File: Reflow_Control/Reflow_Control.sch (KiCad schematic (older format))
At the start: 35 parts

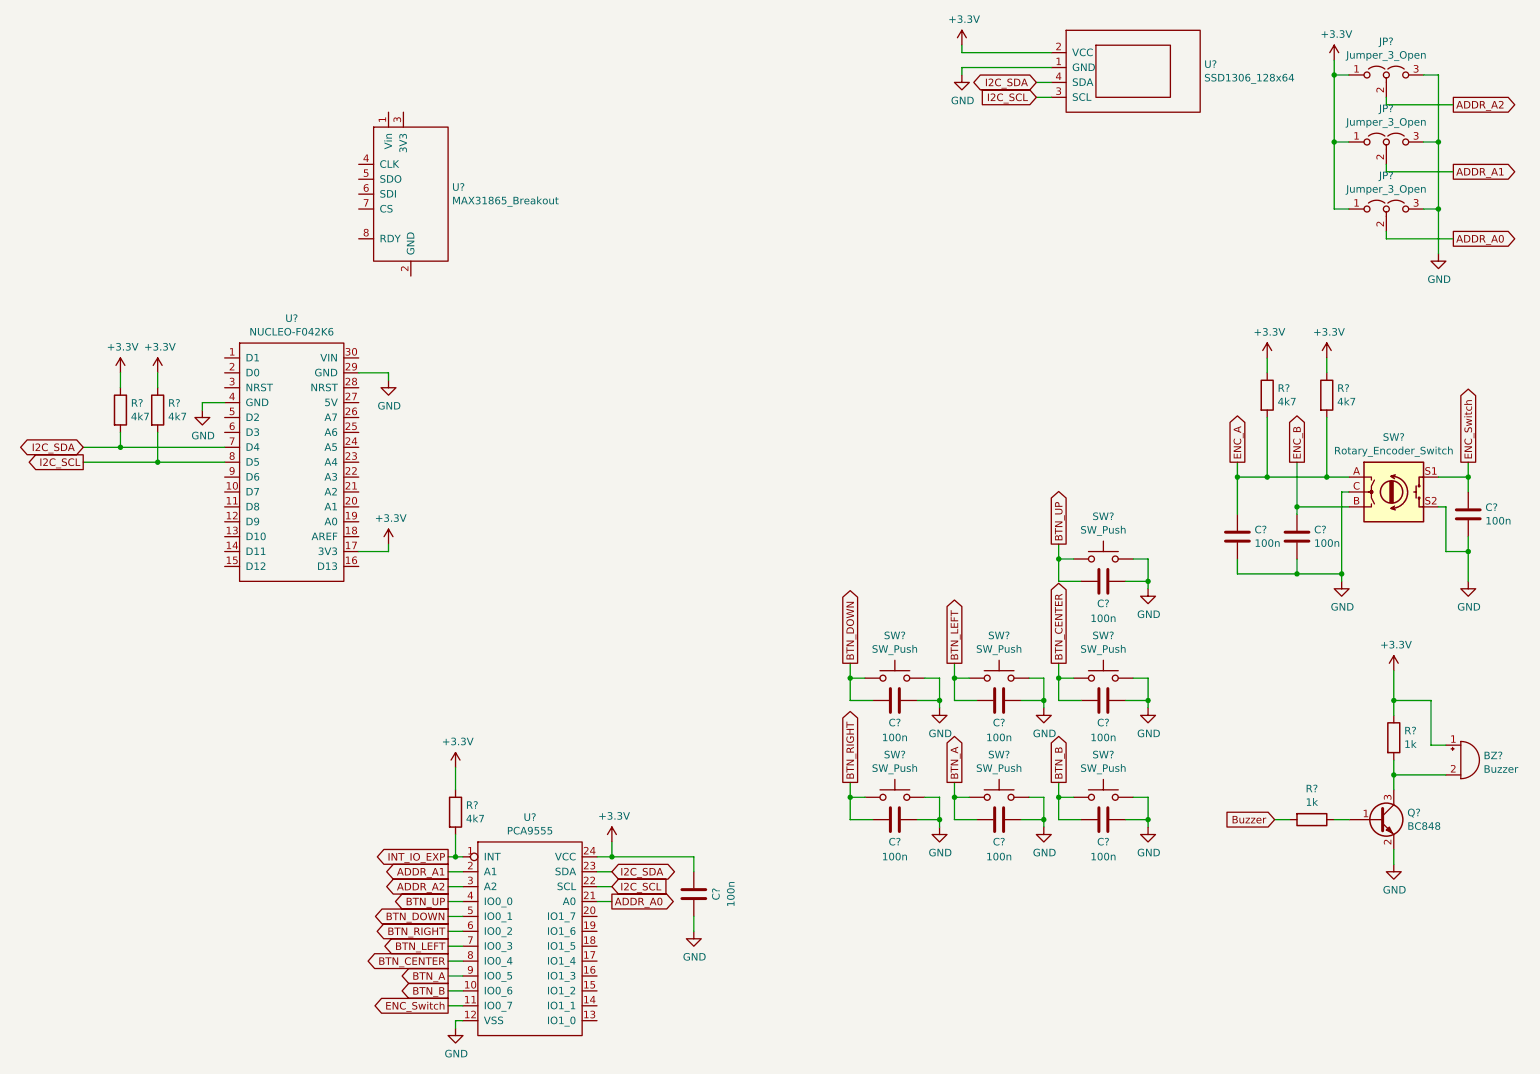
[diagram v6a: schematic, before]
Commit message: working on MAX31865
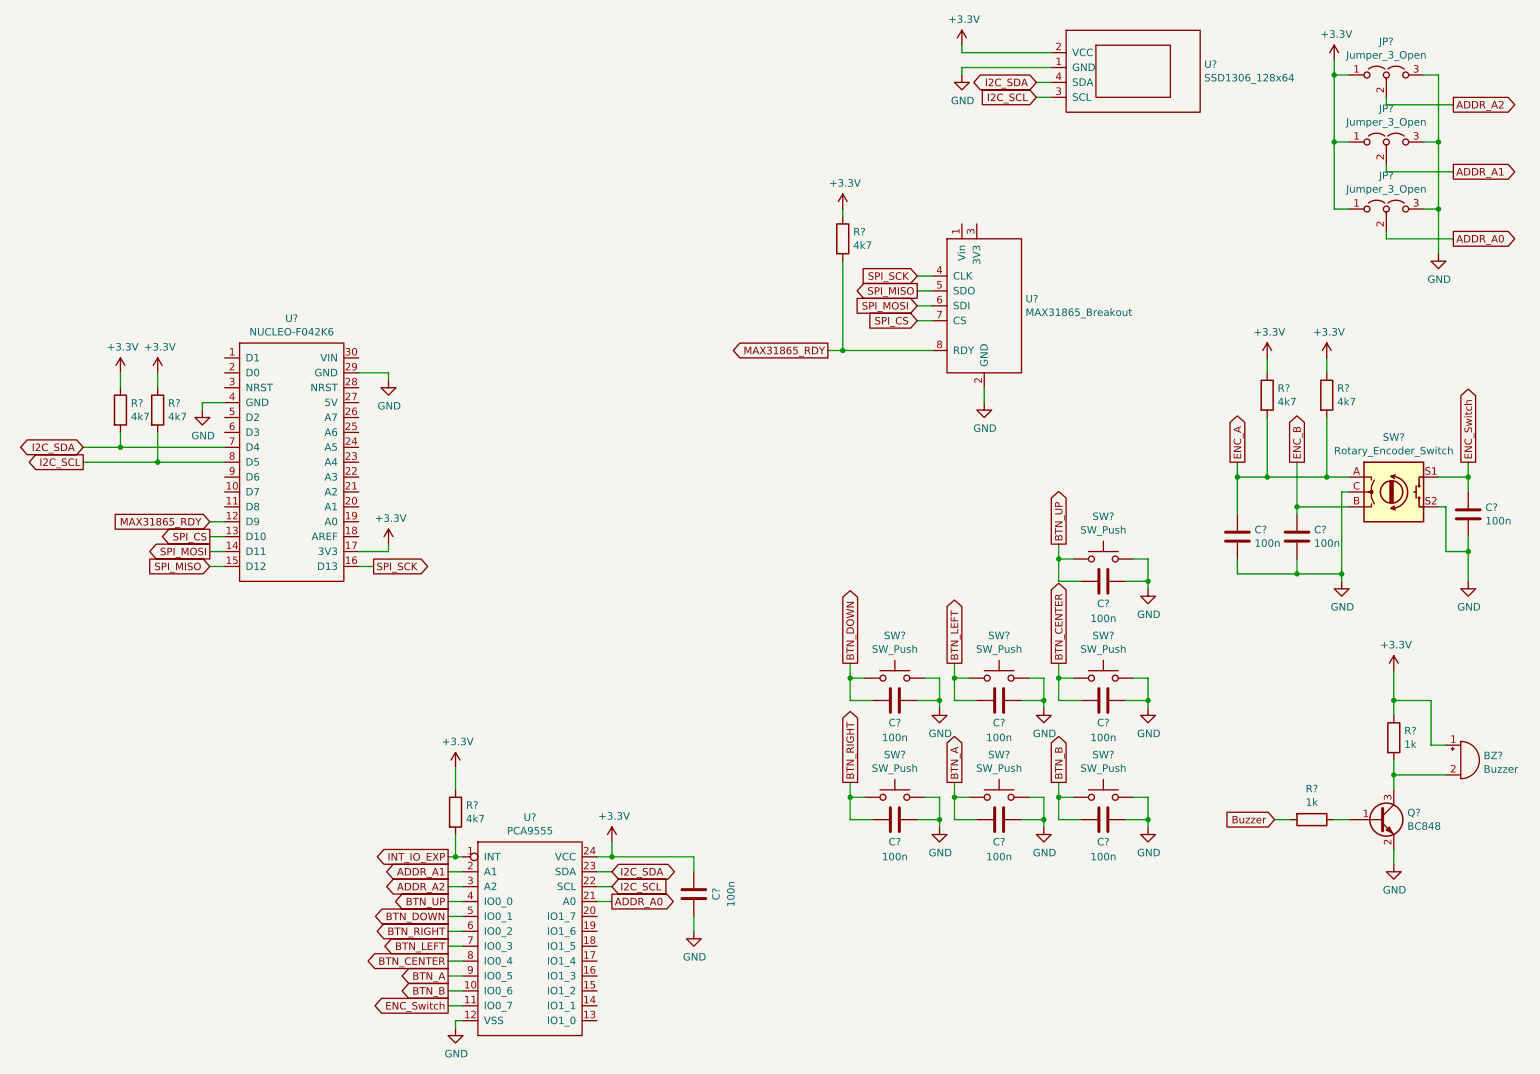
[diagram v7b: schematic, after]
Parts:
- added R?: 4k7, Resistor_SMD:R_1206_3216Metric_Pad1.42x1.75mm_HandSolder, symbol Device:R
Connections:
- net +3V3: now also R?.1
- net GND: now also U?.2 (GND)
- net MAX31865_RDY: now reaches U?.12 (D9)
- net MAX31865_RDY: now also U?.8 (RDY), R?.2
- net SPI_CS: now reaches U?.13 (D10)
- net SPI_CS: now also U?.7 (CS)
- net SPI_MOSI: now reaches U?.14 (D11)
- net SPI_MOSI: now also U?.6 (SDI)
- net SPI_MISO: now reaches U?.15 (D12)
- net SPI_MISO: now also U?.5 (SDO)
- net SPI_SCK: now reaches U?.16 (D13)
- net SPI_SCK: now also U?.4 (CLK)
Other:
- moved on the sheet: U?
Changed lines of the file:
@@
 L Reflow_Control-rescue:MAX31865_Breakout-my_lib U?
 U 1 1 5F6E1D4F
-P 3750 1850
-F 0 "U?" H 3977 1946 50  0000 L CNN
-F 1 "MAX31865_Breakout" H 3977 1855 50  0000 L CNN
-F 2 "MY_FOOTPRINT:MAX31865_Breakout" H 3750 1850 50  0001 C CNN
-F 3 "" H 3750 1850 50  0001 C CNN
-	1    3750 1850
+P 7600 2600
+F 0 "U?" H 7827 2696 50  0000 L CNN
+F 1 "MAX31865_Breakout" H 7827 2605 50  0000 L CNN
+F 2 "MY_FOOTPRINT:MAX31865_Breakout" H 7600 2600 50  0001 C CNN
+F 3 "" H 7600 2600 50  0001 C CNN
+	1    7600 2600
 	1    0    0    -1
 $EndComp
@@
 Wire Wire Line
 	7400 850  8000 850
+$Comp
+L power:GND #PWR?
+U 1 1 5FB410E8
+P 7550 3200
+F 0 "#PWR?" H 7550 2950 50  0001 C CNN
+F 1 "GND" H 7555 3027 50  0000 C CNN
+F 2 "" H 7550 3200 50  0001 C CNN
+F 3 "" H 7550 3200 50  0001 C CNN
+	1    7550 3200
+	1    0    0    -1
+$EndComp
+Wire Wire Line
+	7550 3200 7550 3100
+Text GLabel 2350 4200 0    50   Output ~ 0
+SPI_MOSI
+Text GLabel 2350 4300 0    50   Input ~ 0
+SPI_MISO
+Text GLabel 3450 4300 2    50   Output ~ 0
+SPI_SCK
+Wire Wire Line
+	3450 4300 3350 4300
+Wire Wire Line
+	2350 4200 2450 4200
+Wire Wire Line
+	2350 4300 2450 4300
+Text GLabel 7100 2550 0    50   Input ~ 0
+SPI_MOSI
+Text GLabel 7100 2450 0    50   Output ~ 0
+SPI_MISO
+Text GLabel 7100 2350 0    50   Input ~ 0
+SPI_SCK
+Text GLabel 2350 4100 0    50   Output ~ 0
+SPI_CS
+Wire Wire Line
+	2350 4100 2450 4100
+Text GLabel 7100 2650 0    50   Input ~ 0
+SPI_CS
+Wire Wire Line
+	7100 2650 7200 2650
+Wire Wire Line
+	7100 2350 7200 2350
+Wire Wire Line
+	7200 2450 7100 2450
+Text GLabel 2350 4000 0    50   Input ~ 0
+MAX31865_RDY
+Wire Wire Line
+	7100 2550 7200 2550
+Wire Wire Line
+	2350 4000 2450 4000
+Text GLabel 6500 2850 0    50   Output ~ 0
+MAX31865_RDY
+Wire Wire Line
+	6500 2850 6600 2850
+$Comp
+L Device:R R?
+U 1 1 5FB9E607
+P 6600 2100
+F 0 "R?" H 6670 2146 50  0000 L CNN
+F 1 "4k7" H 6670 2055 50  0000 L CNN
+F 2 "Resistor_SMD:R_1206_3216Metric_Pad1.42x1.75mm_HandSolder" V 6530 2100 50  0001 C CNN
+F 3 "~" H 6600 2100 50  0001 C CNN
+F 4 "Rhom" H 6600 2100 50  0001 C CNN "Man"
+F 5 "KTR18EZPF4701" H 6600 2100 50  0001 C CNN "Man no"
+F 6 "Digikey" H 6600 2100 50  0001 C CNN "Dist"
+F 7 "RHM4.7KAICT-ND" H 6600 2100 50  0001 C CNN "Dist no"
+	1    6600 2100
+	1    0    0    -1
+$EndComp
+Wire Wire Line
+	6600 2250 6600 2850
+Connection ~ 6600 2850
+Wire Wire Line
+	6600 2850 7200 2850
+$Comp
+L power:+3.3V #PWR?
+U 1 1 5FBAEDD7
+P 6600 1900
+F 0 "#PWR?" H 6600 1750 50  0001 C CNN
+F 1 "+3.3V" H 6615 2073 50  0000 C CNN
+F 2 "" H 6600 1900 50  0001 C CNN
+F 3 "" H 6600 1900 50  0001 C CNN
+	1    6600 1900
+	1    0    0    -1
+$EndComp
+Wire Wire Line
+	6600 1900 6600 1950
 $EndSCHEMATC

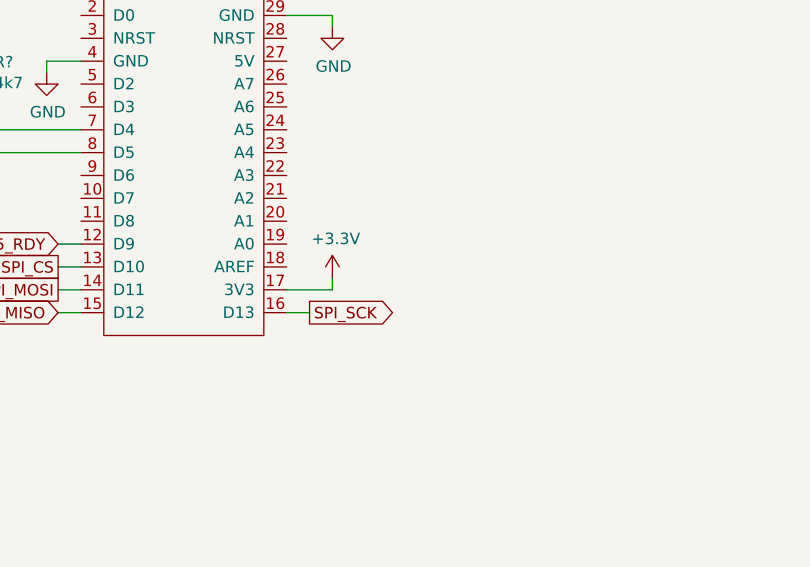
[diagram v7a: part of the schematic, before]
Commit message: connected Encoder to A0and A1(PA0, PA1)
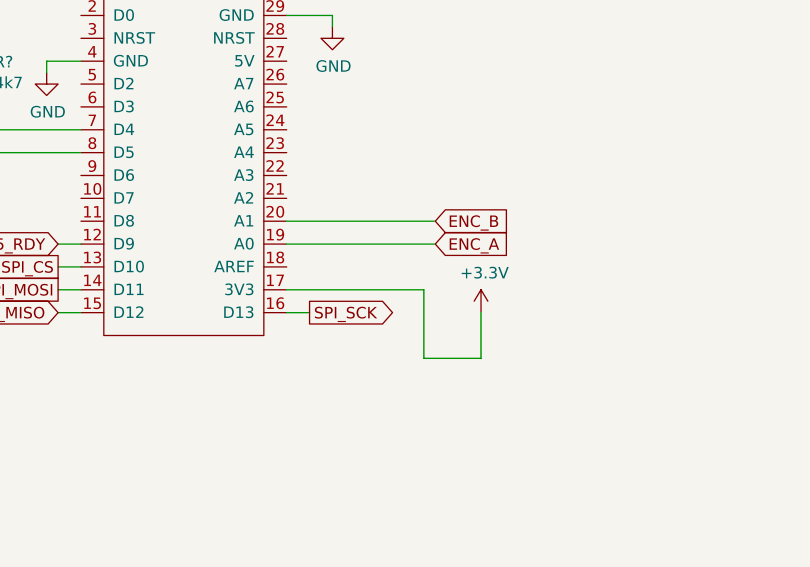
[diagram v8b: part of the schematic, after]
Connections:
- net ENC_A: now also U?.19 (A0)
- net ENC_B: now also U?.20 (A1)
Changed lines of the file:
@@
 L power:+3.3V #PWR?
 U 1 1 5FB04176
-P 3550 4150
-F 0 "#PWR?" H 3550 4000 50  0001 C CNN
-F 1 "+3.3V" H 3565 4323 50  0000 C CNN
-F 2 "" H 3550 4150 50  0001 C CNN
-F 3 "" H 3550 4150 50  0001 C CNN
-	1    3550 4150
+P 4200 4300
+F 0 "#PWR?" H 4200 4150 50  0001 C CNN
+F 1 "+3.3V" H 4215 4473 50  0000 C CNN
+F 2 "" H 4200 4300 50  0001 C CNN
+F 3 "" H 4200 4300 50  0001 C CNN
+	1    4200 4300
 	1    0    0    -1
 $EndComp
-Wire Wire Line
-	3350 4200 3550 4200
-Wire Wire Line
-	3550 4200 3550 4150
 $Comp
 L power:GND #PWR?
@@
 Wire Wire Line
 	6600 1900 6600 1950
+Text GLabel 4000 4000 2    50   Input ~ 0
+ENC_A
+Text GLabel 4000 3900 2    50   Input ~ 0
+ENC_B
+Wire Wire Line
+	3350 3900 4000 3900
+Wire Wire Line
+	4000 4000 3350 4000
+Wire Wire Line
+	3350 4200 3950 4200
+Wire Wire Line
+	3950 4200 3950 4500
+Wire Wire Line
+	3950 4500 4200 4500
+Wire Wire Line
+	4200 4500 4200 4300
 $EndSCHEMATC
